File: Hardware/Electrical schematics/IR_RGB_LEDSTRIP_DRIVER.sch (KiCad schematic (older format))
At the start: 25 parts, among them J1 Barrel_Jack, J2 Conn_01x04_Female, J3 ICSP connector, Q1 IRLZ34N, Q2 IRLZ34N, Q3 IRLZ34N, SW1 SW_RESET, U1 TSOP134xx, U2 L7805, U3 ATmega328P-PU

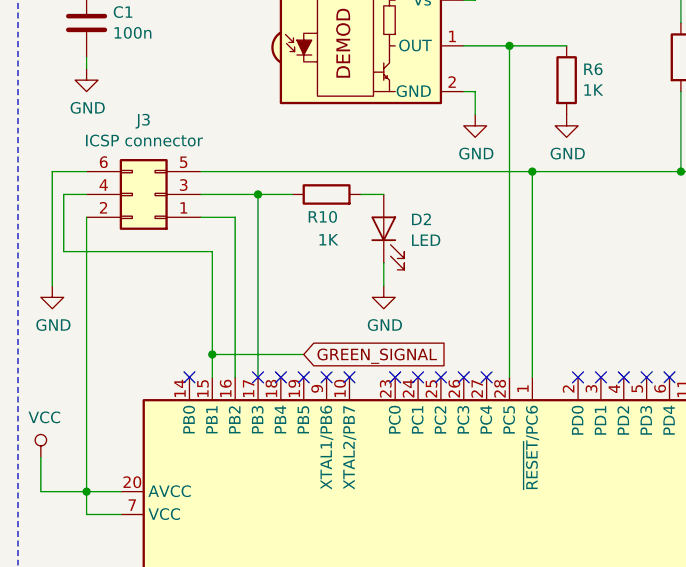
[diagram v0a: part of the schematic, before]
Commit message: Fixed connection error for the ICSP port
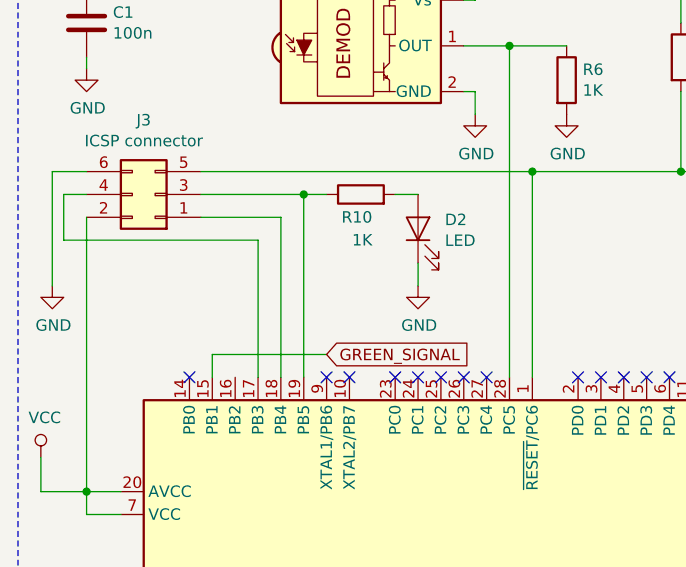
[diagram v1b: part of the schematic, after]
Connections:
- net GREEN_SIGNAL: no longer J3.4 (Pin_4)
- net at U3.16 (PB2): no longer J3.1 (Pin_1)
- net at J3.3 (Pin_3), R10.1: now also U3.19 (PB5); no longer U3.17 (PB3)
- net at U3.18 (PB4): now also J3.1 (Pin_1)
- new net: J3.4 (Pin_4), U3.17 (PB3)
- no-connect marks 17 -> 14
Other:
- moved on the sheet: D2, R10
